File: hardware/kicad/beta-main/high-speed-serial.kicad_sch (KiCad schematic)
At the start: 1 part

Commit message: 5V and amplifier corrections
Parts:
- renumbered Module2 to Module1
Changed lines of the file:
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@@
 		(dnp no)
 		(fields_autoplaced yes)
-		(property "Reference" "Module2"
+		(property "Reference" "Module1"
 			(at 101.6 33.02 0)
 			(effects
@@
 			(project "beta-main"
 				(path "/ec75fd42-4efa-4f32-b57e-76d632cb46f5/b3cf40a7-4d41-420e-a440-2c08f4160b31/73aabdab-ec7c-4b05-9a0f-ff93ba2e60b6"
-					(reference "Module2")
+					(reference "Module1")
 					(unit 2)
 				)

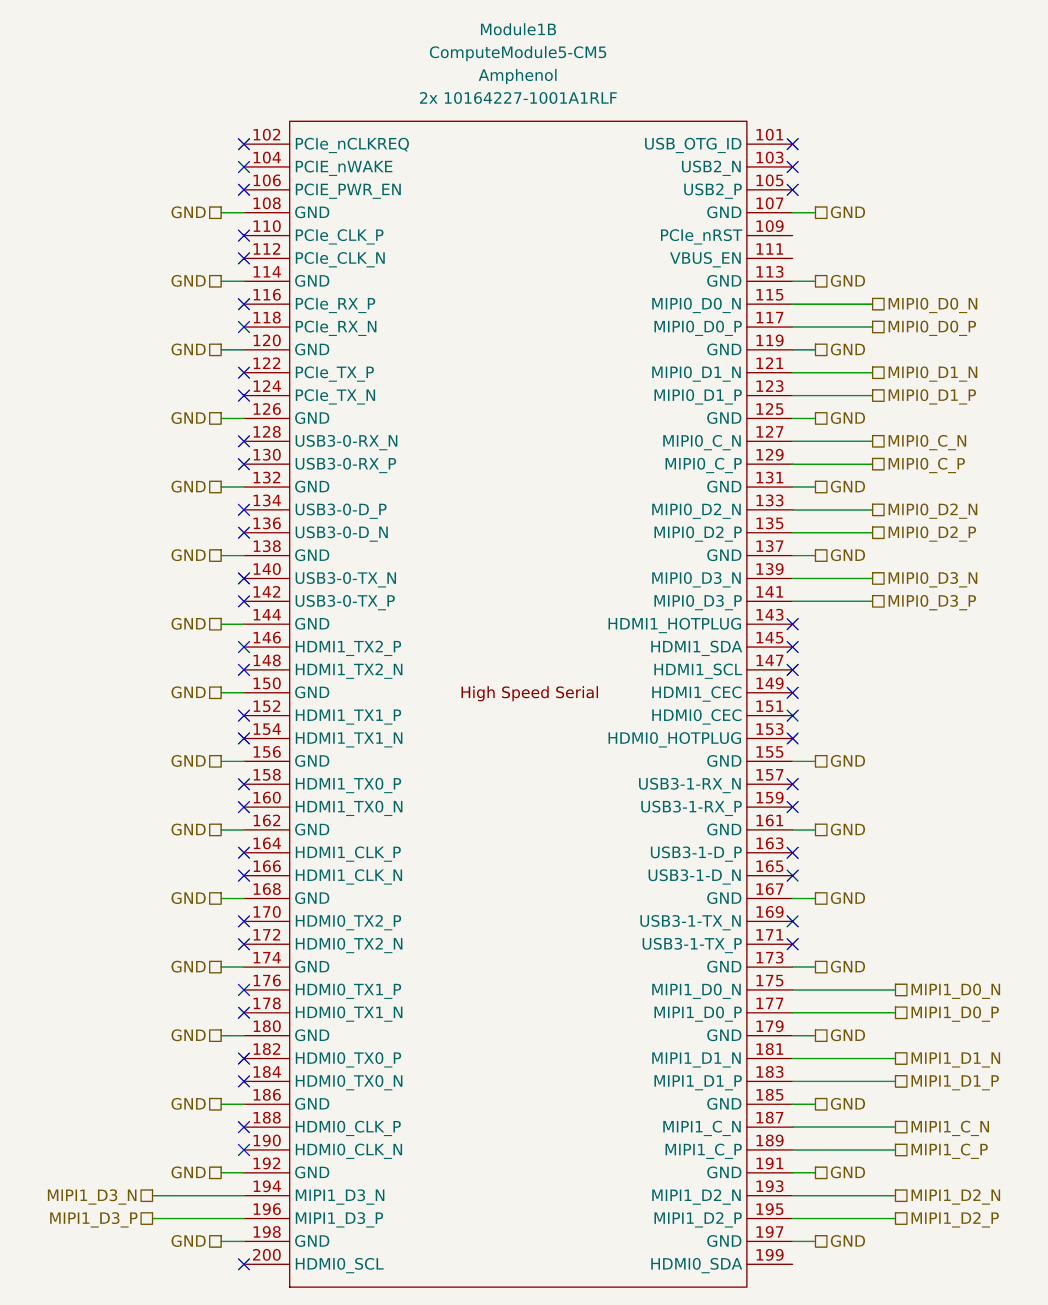
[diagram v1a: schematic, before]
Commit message: Amplifier set for left channel only and god rid of all errors from ERC
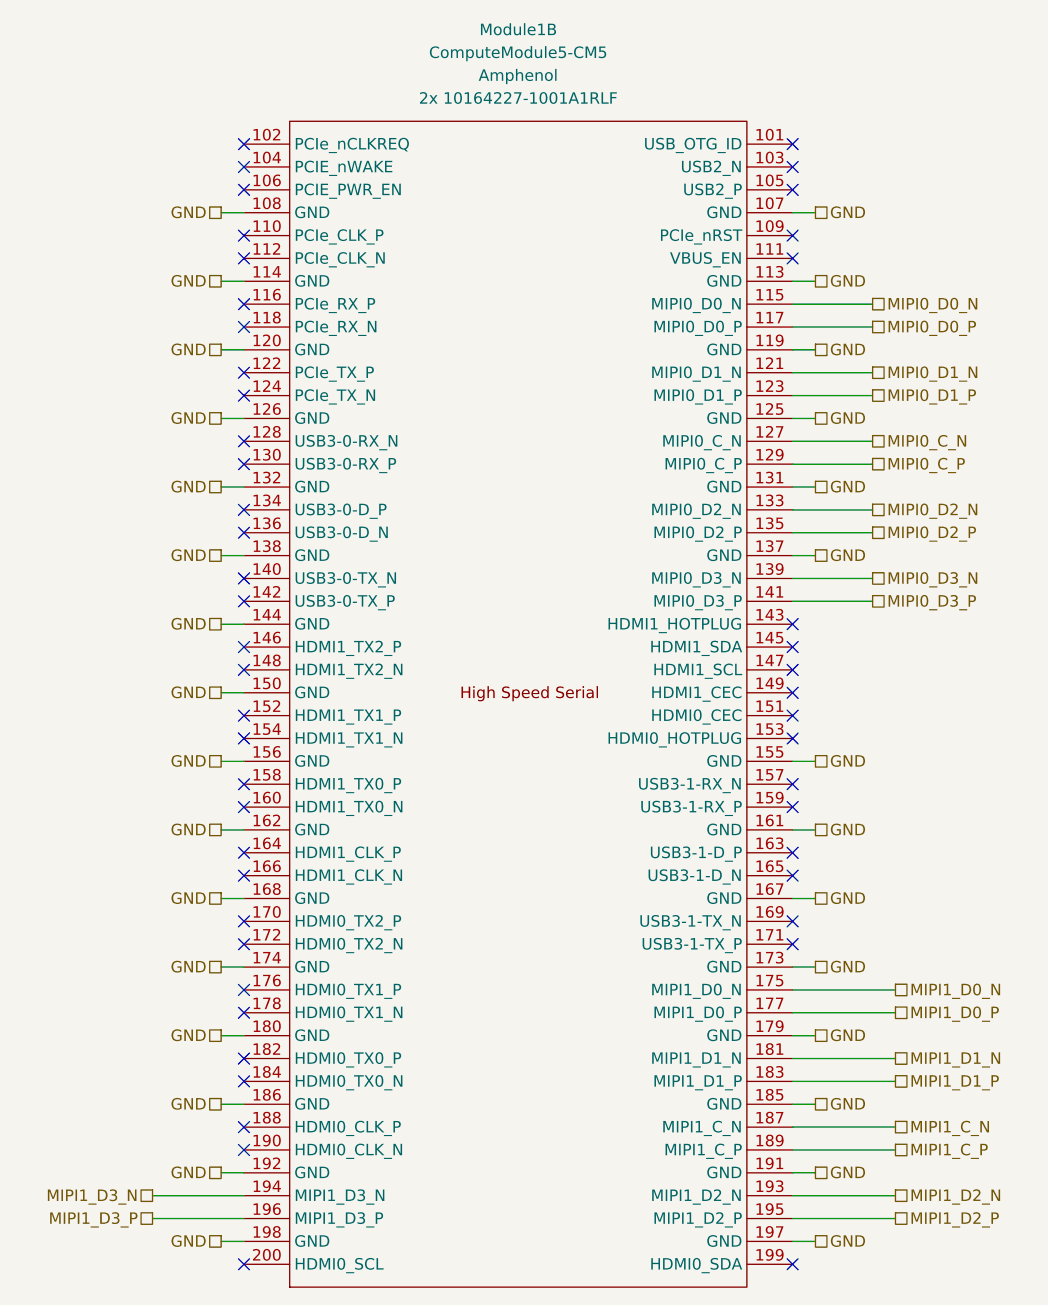
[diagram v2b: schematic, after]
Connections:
- no-connect marks 47 -> 50
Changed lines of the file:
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@@
+	)
+	(no_connect
+		(at 132.08 55.88)
 	)
 	(no_connect
@@
 	)
 	(no_connect
+		(at 132.08 170.18)
+	)
+	(no_connect
 		(at 71.12 71.12)
 	)
@@
 	)
 	(no_connect
+		(at 132.08 58.42)
+	)
+	(no_connect

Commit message: remove power symbols from hierarchy and move different subsystems  around
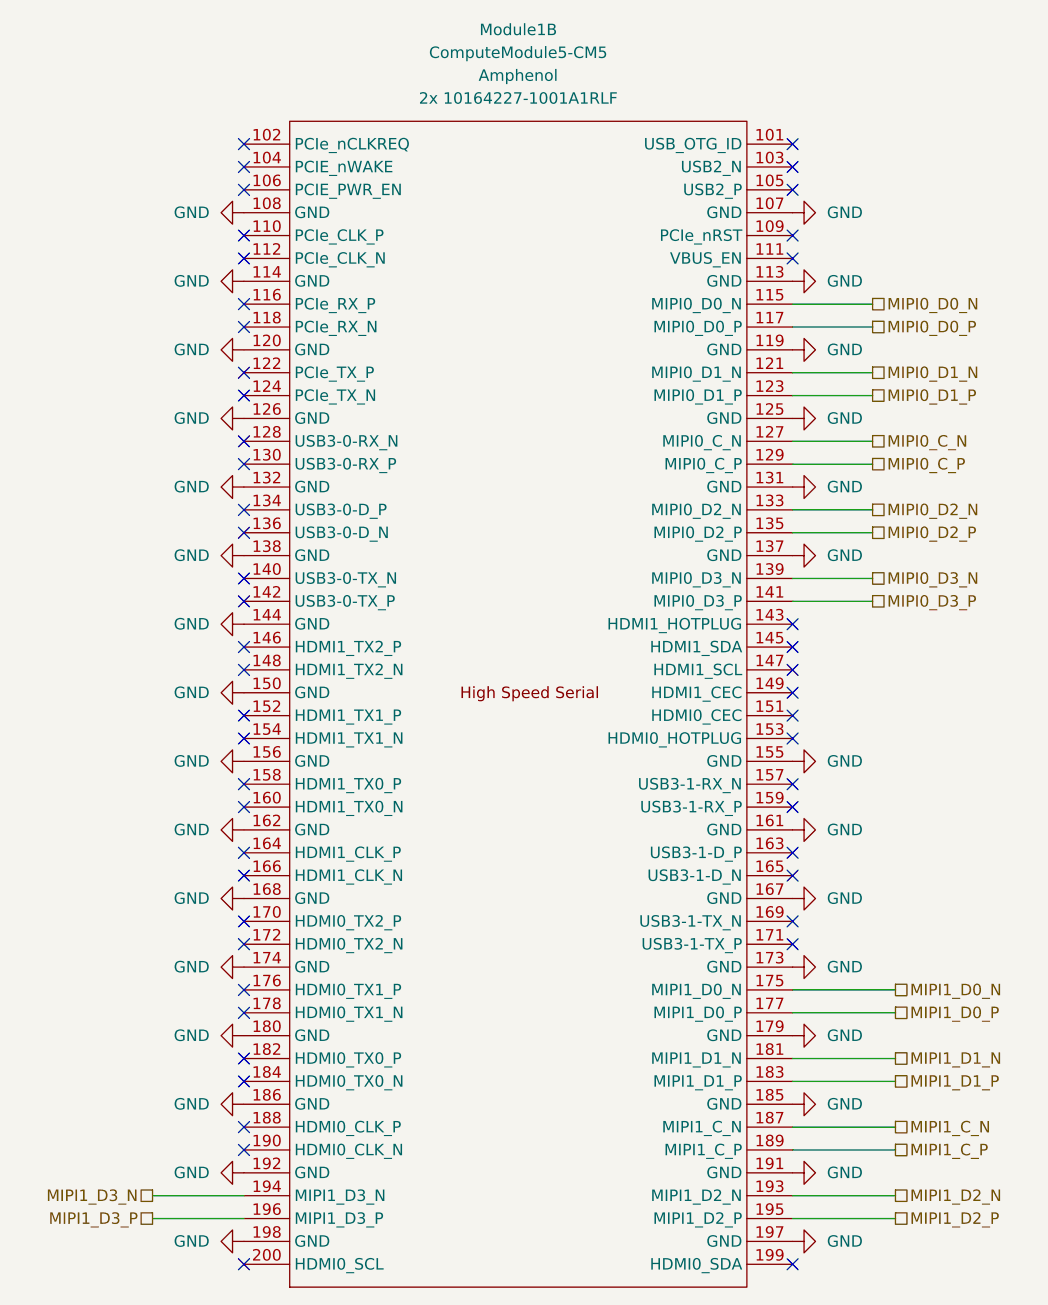
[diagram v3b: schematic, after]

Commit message: add modifications
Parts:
- removed Module1: ComputeModule5-CM5, CM5IO:Raspberry-Pi-5-Compute-Module, symbol CM5IO:ComputeModule5-CM5
- added CM5: ComputeModule5-CM5, CM5IO:Raspberry-Pi-5-Compute-Module, symbol CM5IO:ComputeModule5-CM5
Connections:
- net GND: now also CM5.107 (GND), CM5.108 (GND), CM5.113 (GND), CM5.114 (GND), CM5.119 (GND), CM5.120 (GND), CM5.125 (GND), CM5.126 (GND), CM5.131 (GND), CM5.132 (GND), CM5.137 (GND), CM5.138 (GND), CM5.144 (GND), CM5.150 (GND), CM5.155 (GND), CM5.156 (GND), CM5.161 (GND), CM5.162 (GND), CM5.167 (GND), CM5.168 (GND), CM5.173 (GND), CM5.174 (GND), CM5.179 (GND), CM5.180 (GND), CM5.185 (GND), CM5.186 (GND), CM5.191 (GND), CM5.192 (GND), CM5.197 (GND), CM5.198 (GND)
- net MIPI0_C_N: now also CM5.127 (MIPI0_C_N)
- net MIPI0_C_P: now also CM5.129 (MIPI0_C_P)
- net MIPI0_D0_N: now also CM5.115 (MIPI0_D0_N)
- net MIPI0_D0_P: now also CM5.117 (MIPI0_D0_P)
- net MIPI0_D1_N: now also CM5.121 (MIPI0_D1_N)
- net MIPI0_D1_P: now also CM5.123 (MIPI0_D1_P)
- net MIPI0_D2_N: now also CM5.133 (MIPI0_D2_N)
- net MIPI0_D2_P: now also CM5.135 (MIPI0_D2_P)
- net MIPI0_D3_N: now also CM5.139 (MIPI0_D3_N)
- net MIPI0_D3_P: now also CM5.141 (MIPI0_D3_P)
- net MIPI1_C_N: now also CM5.187 (MIPI1_C_N)
- net MIPI1_C_P: now also CM5.189 (MIPI1_C_P)
- net MIPI1_D0_N: now also CM5.175 (MIPI1_D0_N)
- net MIPI1_D0_P: now also CM5.177 (MIPI1_D0_P)
- net MIPI1_D1_N: now also CM5.181 (MIPI1_D1_N)
- net MIPI1_D1_P: now also CM5.183 (MIPI1_D1_P)
- net MIPI1_D2_N: now also CM5.193 (MIPI1_D2_N)
- net MIPI1_D2_P: now also CM5.195 (MIPI1_D2_P)
- net MIPI1_D3_N: now also CM5.194 (MIPI1_D3_N)
- net MIPI1_D3_P: now also CM5.196 (MIPI1_D3_P)
- new net USB3-0-D_N: CM5.136 (USB3-0-D_N)
- new net USB3-0-D_P: CM5.134 (USB3-0-D_P)
- new net USB3-0-RX_N: CM5.128 (USB3-0-RX_N)
- new net USB3-0-RX_P: CM5.130 (USB3-0-RX_P)
- new net USB3-0-TX_N: CM5.140 (USB3-0-TX_N)
- new net USB3-0-TX_P: CM5.142 (USB3-0-TX_P)
- new net USB3-1-D_N: CM5.165 (USB3-1-D_N)
- new net USB3-1-D_P: CM5.163 (USB3-1-D_P)
- new net USB3-1-RX_N: CM5.157 (USB3-1-RX_N)
- new net USB3-1-RX_P: CM5.159 (USB3-1-RX_P)
- new net USB3-1-TX_N: CM5.169 (USB3-1-TX_N)
- new net USB3-1-TX_P: CM5.171 (USB3-1-TX_P)
- new net VBUS_EN: CM5.111 (VBUS_EN)
- no-connect marks 50 -> 37
